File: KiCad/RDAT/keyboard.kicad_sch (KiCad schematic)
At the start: 242 parts, among them J1 Conn_01x02, J2 Conn_01x02, U1 SC091413, U2 W25Q128JVS, X1 ABM8-272-T3

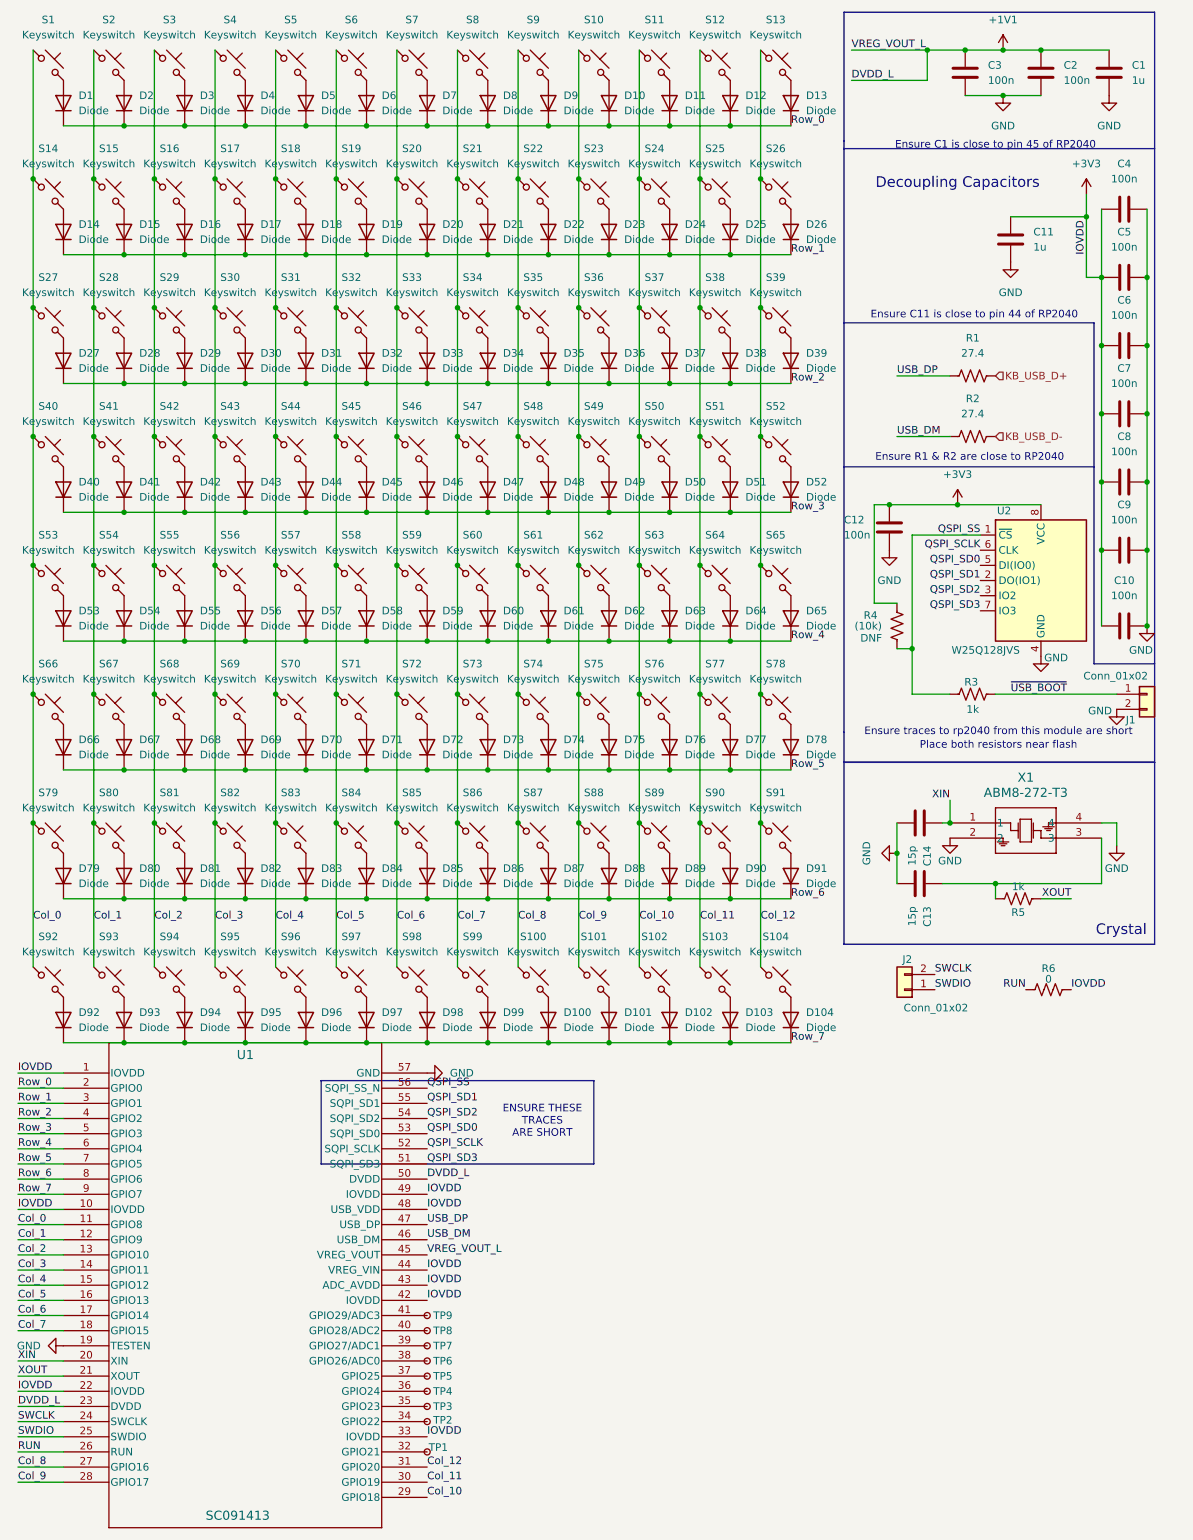
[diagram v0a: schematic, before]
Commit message: Add new notes; update component references in schematics and footprints, and complete charging design
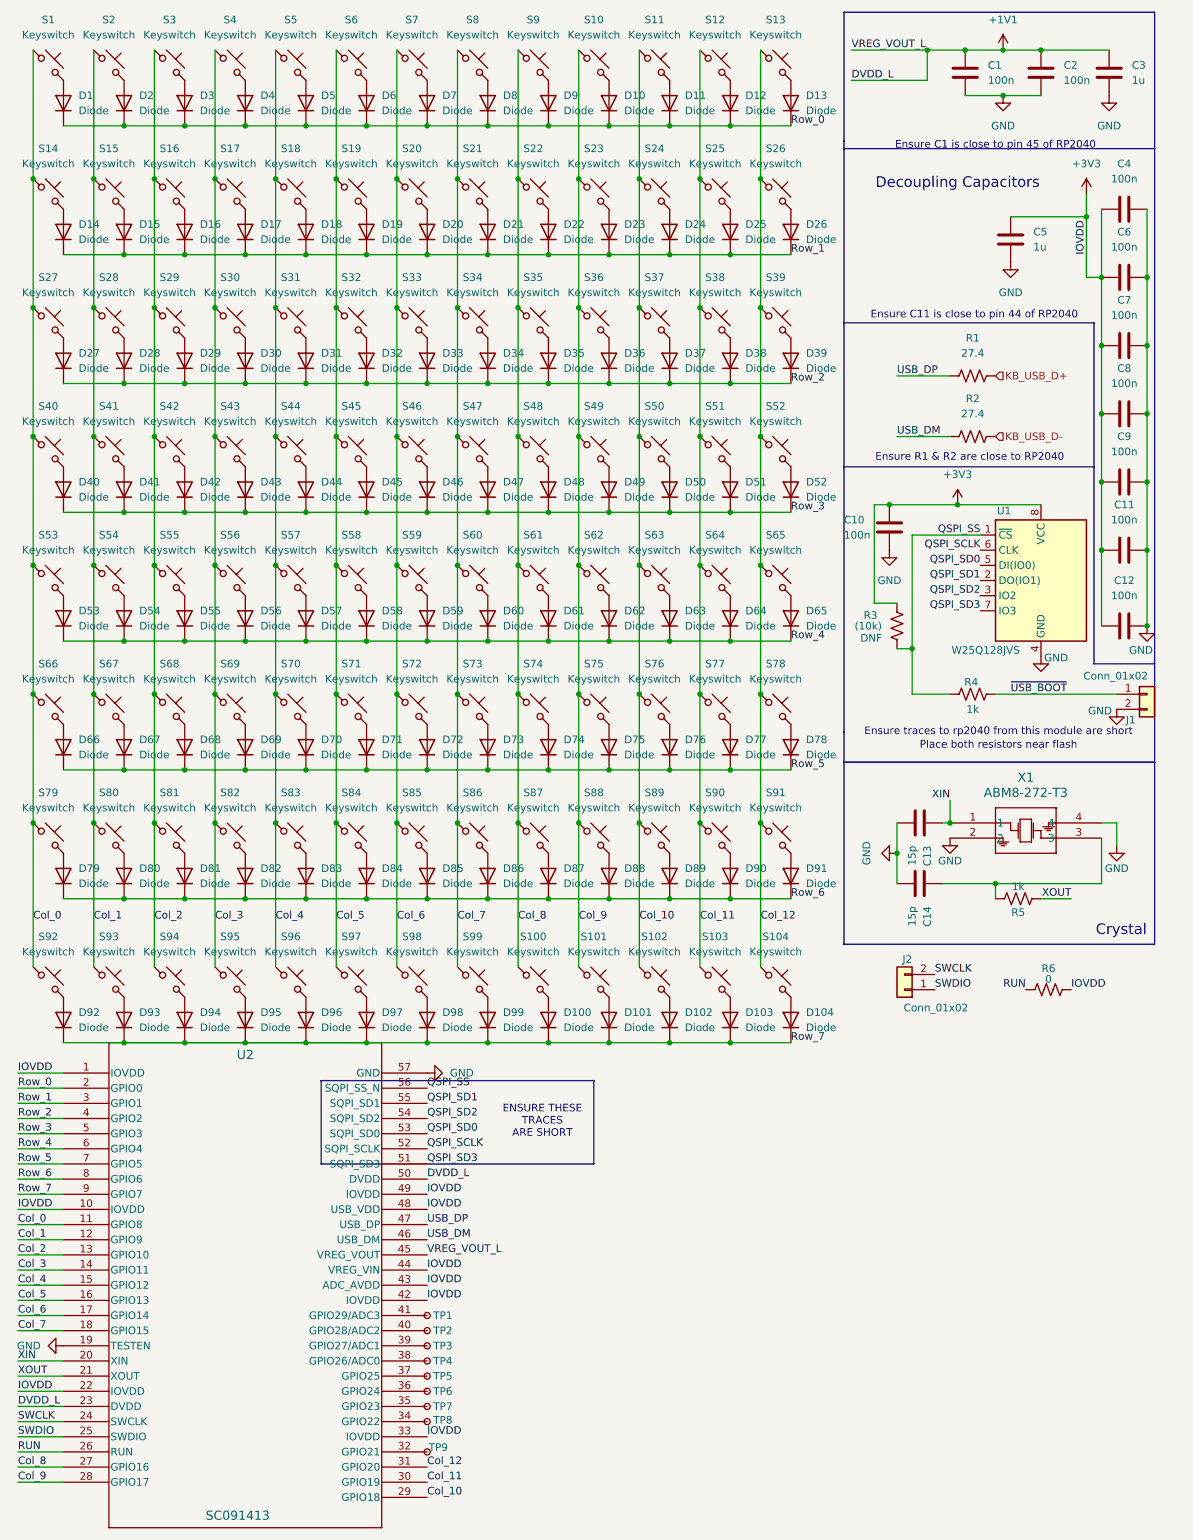
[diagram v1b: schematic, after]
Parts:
- renumbered C3 to C1, C12 to C10, C9 to C11, C10 to C12, C14 to C13, C13 to C14, C1 to C3, C11 to C5, C5 to C6, C6 to C7, C7 to C8, C8 to C9, R4 to R3, R3 to R4, TP9 to TP1, TP8 to TP2, TP7 to TP3, TP6 to TP4, TP4 to TP6, TP3 to TP7, TP2 to TP8, TP1 to TP9, U2 to U1, U1 to U2

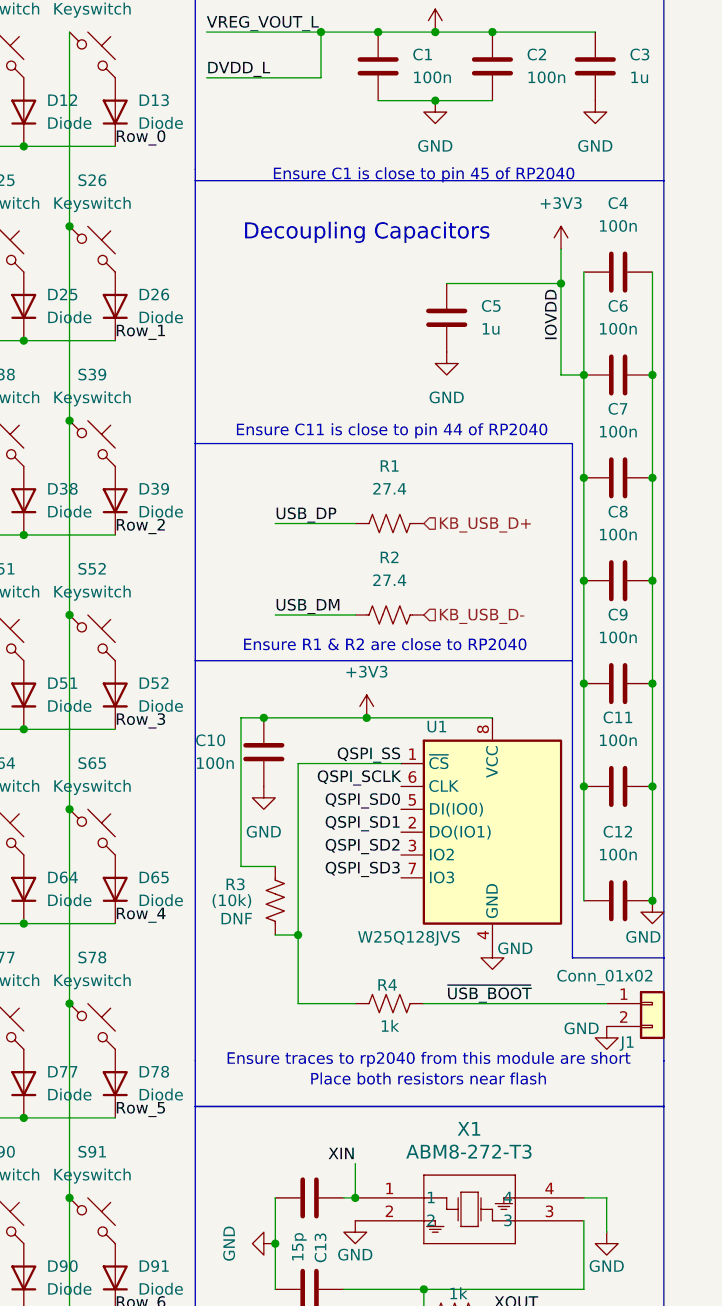
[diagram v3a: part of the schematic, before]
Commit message: Added Libs and DOCS
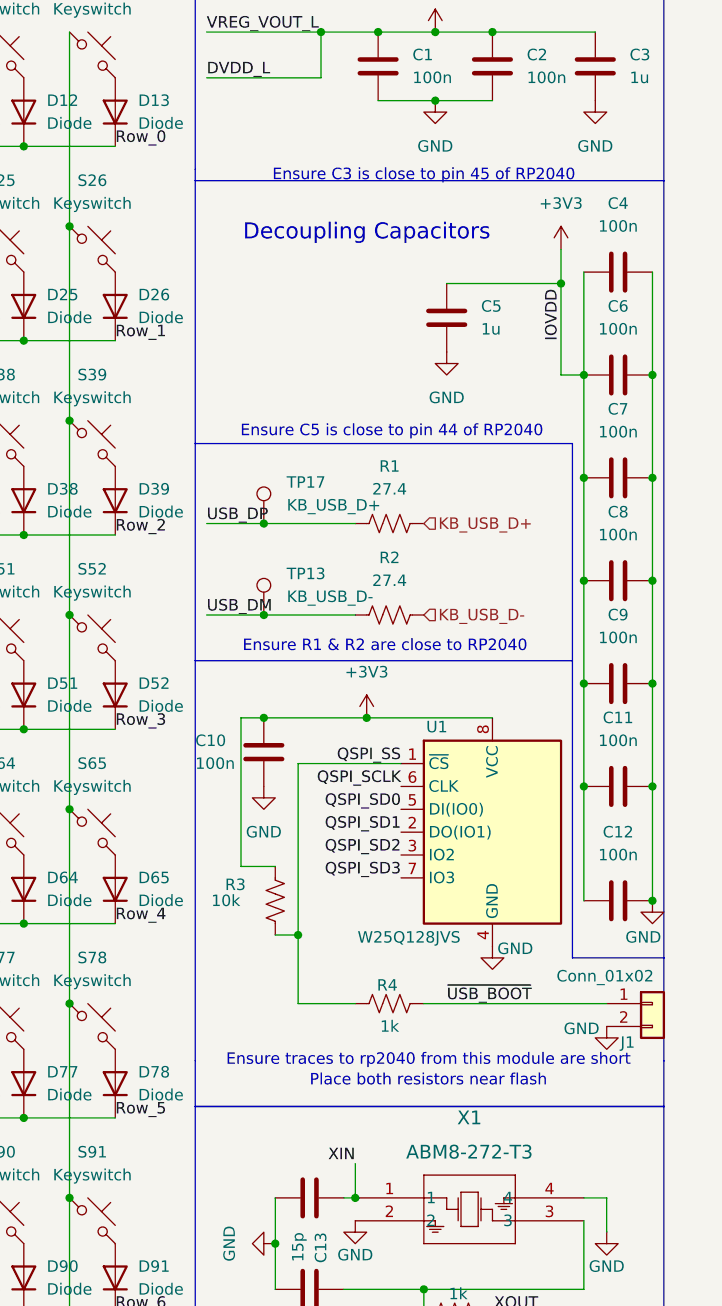
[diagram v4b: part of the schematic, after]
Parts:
- added TP13: KB_USB_D-, TestPoint:TestPoint_Loop_D1.80mm_Drill1.0mm_Beaded, symbol Connector:TestPoint
- added TP17: KB_USB_D+, TestPoint:TestPoint_Loop_D1.80mm_Drill1.0mm_Beaded, symbol Connector:TestPoint
- C1, C10, C11, C12, C2, C3, C4, C5, C6, C7, C8, C9: footprint (none) -> Capacitor_SMD:C_0402_1005Metric; JLCPCB_LINK (none) -> https://jlcpcb.com/partdetail/1877-CL05B104KO5NNNC/C1525
- C13, C14: footprint (none) -> Capacitor_SMD:C_0402_1005Metric; JLCPCB_LINK (none) -> https://jlcpcb.com/partdetail/87461-CL05C150JB5NNNC/C86285
- D1, D10, D100, D101, D102, D103, D104, D11, D12, D13, D14, D15, D16, D17, D18, D19, D2, D20, D21, D22, D23, D24, D25, D26, D27, D28, D29, D3, D30, D31, D32, D33, D34, D35, D36, D37, D38, D39, D4, D40, D41, D42, D43, D44, D45, D46, D47, D48, D49, D5, D50, D51, D52, D53, D54, D55, D56, D57, D58, D59, D6, D60, D61, D62, D63, D64, D65, D66, D67, D68, D69, D7, D70, D71, D72, D73, D74, D75, D76, D77, D78, D79, D8, D80, D81, D82, D83, D84, D85, D86, D87, D88, D89, D9, D90, D91, D92, D93, D94, D95, D96, D97, D98, D99: footprint (none) -> Diode_SMD:D_MiniMELF; JLCPCB_LINK (none) -> https://jlcpcb.com/partdetail/Yongyutai-LL4148/C2891733
- J1, J2: footprint (none) -> Connector_PinHeader_1.00mm:PinHeader_1x02_P1.00mm_Vertical; JLCPCB_LINK (none) -> https://www.digikey.com/en/products/detail/gct/BC020-02-A-0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
- R1, R2: footprint (none) -> Resistor_SMD:R_0402_1005Metric; JLCPCB_LINK (none) -> https://jlcpcb.com/partdetail/25843-0402WGF270JTCE/C25100
- R3: value (10k) -> 10k; footprint (none) -> Resistor_SMD:R_0402_1005Metric; JLCPCB_LINK (none) -> https://jlcpcb.com/partdetail/26487-0402WGF1002TCE/C25744
- R4, R5: footprint (none) -> Resistor_SMD:R_0402_1005Metric; JLCPCB_LINK (none) -> https://jlcpcb.com/partdetail/12256-0402WGF1001TCE/C11702
- R6: footprint (none) -> Resistor_SMD:R_1206_3216Metric; JLCPCB_LINK (none) -> https://jlcpcb.com/partdetail/18576-1206W4F0000T5E/C17888
- S1, S10, S100, S101, S102, S103, S104, S11, S12, S13, S14, S15, S16, S17, S18, S19, S2, S20, S21, S22, S23, S24, S25, S26, S27, S28, S29, S3, S30, S31, S32, S33, S34, S35, S36, S37, S38, S39, S4, S40, S41, S42, S43, S44, S45, S46, S47, S48, S49, S5, S50, S51, S52, S53, S54, S55, S56, S57, S58, S59, S6, S60, S61, S62, S63, S64, S65, S66, S67, S68, S69, S7, S70, S71, S72, S73, S74, S75, S76, S77, S78, S79, S8, S80, S81, S82, S83, S84, S85, S86, S87, S88, S89, S9, S90, S91, S92, S93, S94, S95, S96, S97, S98, S99: footprint (none) -> footprints:SW_PG151101S11
- TP1, TP2, TP3, TP4, TP5, TP6, TP7, TP8, TP9: footprint (none) -> TestPoint:TestPoint_Pad_D1.0mm
- U1: JLCPCB_LINK (none) -> https://jlcpcb.com/partdetail/WinbondElec-W25Q128JVSIQ/C975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
- U2: JLCPCB_LINK (none) -> https://jlcpcb.com/partdetail/RaspberryPi-RP2040/C2040
- X1: JLCPCB_LINK (none) -> https://jlcpcb.com/parts/componentSearch?searchTxt=ABM8-272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
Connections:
- net USB_DM: now also TP13.1
- net USB_DP: now also TP17.1
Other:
- note added: "Ensure C3 is close to pin 45 of RP2040"
- note added: "Ensure C5 is close to pin 44 of RP2040"
- note removed: "Ensure C1 is close to pin 45 of RP2040"
- note removed: "Ensure C11 is close to pin 44 of RP2040"

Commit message: Sourced and documented all parts
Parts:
- S1, S10, S100, S101, S102, S103, S104, S11, S12, S13, S14, S15, S16, S17, S18, S19, S2, S20, S21, S22, S23, S24, S25, S26, S27, S28, S29, S3, S30, S31, S32, S33, S34, S35, S36, S37, S38, S39, S4, S40, S41, S42, S43, S44, S45, S46, S47, S48, S49, S5, S50, S51, S52, S53, S54, S55, S56, S57, S58, S59, S6, S60, S61, S62, S63, S64, S65, S66, S67, S68, S69, S7, S70, S71, S72, S73, S74, S75, S76, S77, S78, S79, S8, S80, S81, S82, S83, S84, S85, S86, S87, S88, S89, S9, S90, S91, S92, S93, S94, S95, S96, S97, S98, S99: JLCPCB_LINK (none) -> https://www.amazon.com/Hot-swap-CPG151101S11-Mechanical-Key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

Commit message: Push before Board Layout
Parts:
- U1: footprint Package_SO:SOIC-8_5.23x5.23mm_P1.27mm -> footprints:SOIC_128JVSIQ_WIN
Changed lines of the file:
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@@
 			)
 		)
-		(property "Footprint" "Package_SO:SOIC-8_5.23x5.23mm_P1.27mm"
+		(property "Footprint" "footprints:SOIC_128JVSIQ_WIN"
 			(at 184.15 85.09 0)
 			(effects

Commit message: Placed a lot of components
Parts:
- removed D104: Diode, Diode_SMD:D_MiniMELF, symbol ScottoKeebs:Placeholder_Diode
- removed S104: Keyswitch, footprints:SW_PG151101S11, symbol ScottoKeebs:Placeholder_Keyswitch
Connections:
- net Col_12: no longer S13.1, S26.1, S39.1, S52.1, S65.1, S78.1, S91.1
- net GND: now also J1.1 (Pin_1); no longer J1.2 (Pin_2)
- net KB_USB_D+: now also TP17.1
- net KB_USB_D-: now also TP13.1
- net USB_DM: no longer TP13.1
- net USB_DP: no longer TP17.1
- net ~{USB_BOOT}: now also J1.2 (Pin_2); no longer J1.1 (Pin_1)
- new net: S13.1, S26.1, S39.1, S52.1, S65.1, S78.1, S91.1
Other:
- moved on the sheet: TP13, TP17

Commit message: End Of day commit
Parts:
- D1, D10, D100, D101, D102, D103, D11, D12, D13, D14, D15, D16, D17, D18, D19, D2, D20, D21, D22, D23, D24, D25, D26, D27, D28, D29, D3, D30, D31, D32, D33, D34, D35, D36, D37, D38, D39, D4, D40, D41, D42, D43, D44, D45, D46, D47, D48, D49, D5, D50, D51, D52, D53, D54, D55, D56, D57, D58, D59, D6, D60, D61, D62, D63, D64, D65, D66, D67, D68, D69, D7, D70, D71, D72, D73, D74, D75, D76, D77, D78, D79, D8, D80, D81, D82, D83, D84, D85, D86, D87, D88, D89, D9, D90, D91, D92, D93, D94, D95, D96, D97, D98, D99: footprint Diode_SMD:D_MiniMELF -> Diode_SMD:D_SOD-882; symbol ScottoKeebs:Placeholder_Diode -> Device:D_Schottky; JLCPCB_LINK https://jlcpcb.com/partdetail/Yongyutai-LL4148/C2891733 -> https://jlcpcb.com/partdetail/TechPublic-BAT54LTP/C587155
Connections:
- net Col_12: now also S13.1, S26.1, S39.1, S52.1, S65.1, S78.1, S91.1
- net +1V1 renamed DVDD_L
